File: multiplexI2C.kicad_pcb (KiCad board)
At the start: 2 copper layers, 48.3 x 71.1 mm, 92 parts, among them J1 Screw_Terminal_01x04, J101 Screw_Terminal_01x02, J2 Screw_Terminal_01x04, J3 Screw_Terminal_01x04, J4 Screw_Terminal_01x04, J401 Conn_02x04_Top_Bottom, J5 Screw_Terminal_01x04, J6 Screw_Terminal_01x04, J7 Screw_Terminal_01x04, J8 Screw_Terminal_01x04, SW401 RST, SW402 BT0, U1 PCA9548A, U101 AMS1117-3.3 SOT-223, U401 STM32F411CEU6, U701 RFM95W-915S2, Y501 32.758kHz, Y601 25MHz

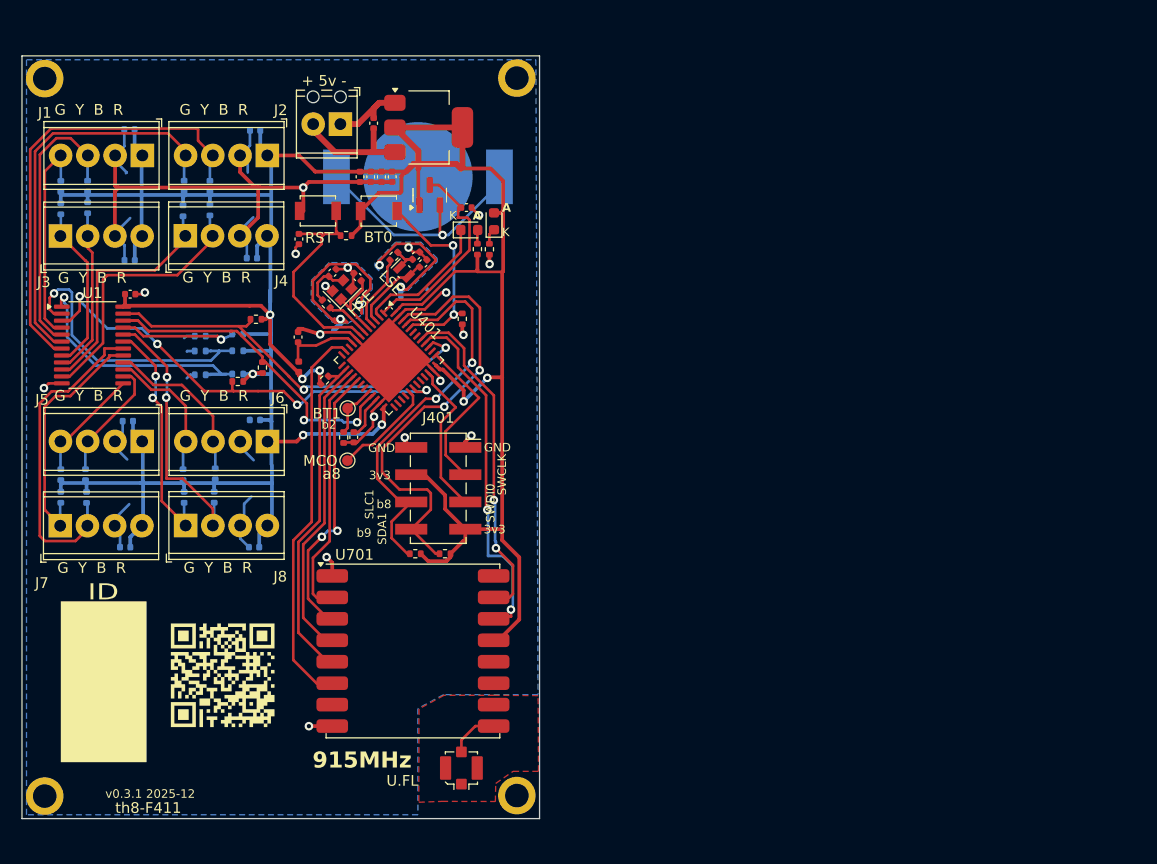
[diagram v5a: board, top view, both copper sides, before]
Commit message: adjusted copper zones and mounting holes for better setback from edge. Fab layers cleanup and some documentation cleanup.
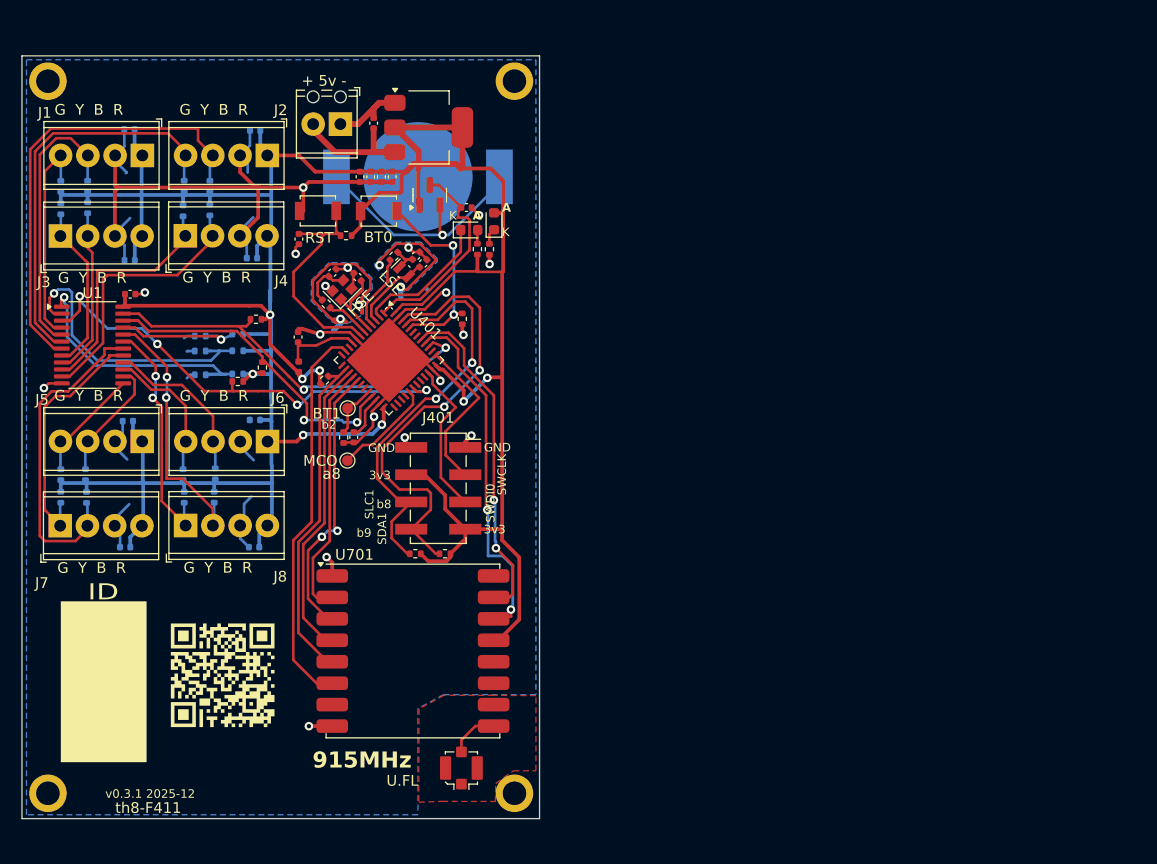
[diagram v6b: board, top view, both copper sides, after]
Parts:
- removed G***: LOGO, ProjectLib:IDblock
- moved H4 0.40 mm to (52.0, 92.9)
- moved H3 0.38 mm to (52.0, 26.5)
- moved H2 0.36 mm to (95.5, 26.5)
- moved H1 0.31 mm to (95.5, 92.9)

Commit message: th8-F411 2025-12 plus some cleanup post manufacturing.
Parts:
- added C107: 10µF, ProjectLib:C_0402_1005Metric, F.Cu at (82.2, 31.9)
- added C108: 10µF, ProjectLib:C_0402_1005Metric, F.Cu at (82.0, 35.4)
- added C12: 100nF, ProjectLib:C_0402_1005Metric, F.Cu at (88.5, 70.5)
- added C13: 10µF, ProjectLib:C_0402_1005Metric, F.Cu at (91.7, 70.5)
- added NT3: NetTie_2, ProjectLib:NetTie-2_SMD_Pad0.5mm, F.Cu at (81.6, 70.3)
- R501: value 0 -> 0k
- SW401: value RST -> SW_Push
- SW402: value BT0 -> SW_Push
- moved C103 14.5 mm to (93.1, 44.8), turned to 90 degrees
- moved R407 2.37 mm to (86.6, 70.6)
- moved R406 1.50 mm to (84.7, 70.6)
- moved C101 0.56 mm to (82.2, 30.9), turned to 180 degrees
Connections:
- U701 pad 1: GND -> GND_RADIO
- U701 pad 8: GND -> GND_RADIO
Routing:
- net GND_ANT: track 0.00 -> 20.8 mm, vias 0 -> 9
- net GND_RADIO: track 0.00 -> 20.1 mm, vias 0 -> 8
- net GND: track 126.5 -> 121.4 mm, vias 15 -> 14
- net +3V3: track 295.7 -> 298.9 mm
- net SDA1: track 41.9 -> 40.4 mm
- net GND_HSE: track 23.4 -> 24.5 mm, vias 4 -> 6
- net Net-(BT101-+): track 23.0 -> 22.3 mm
- net +5V: track 11.3 -> 10.6 mm
- net SCL1: track 36.9 -> 36.2 mm
- added copper zone on B.Cu, net GND_ANT
- added copper zone on B.Cu, net GND_RADIO
- added copper zone on F.Cu, net GND_RADIO
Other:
- board size 48.3 x 71.1 mm -> 48.2 x 71.1 mm

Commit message: superficial adjustments for warnings found by kicaad 10.
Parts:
- moved NT601 0.92 mm to (78.2, 48.8)
